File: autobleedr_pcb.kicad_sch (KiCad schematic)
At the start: 18 parts, among them J1 Barrel_Jack, J10 XT60 Connector, J11 Conn_01x02_Pin, J13 Screw_Terminal_01x08, J2 Conn_01x13_Pin, J3 Conn_01x14_Pin, J4 Conn_01x08_Socket, J7 Screw_Terminal_01x02, J8 Conn_01x02_Pin, J9 Conn_01x02_Pin

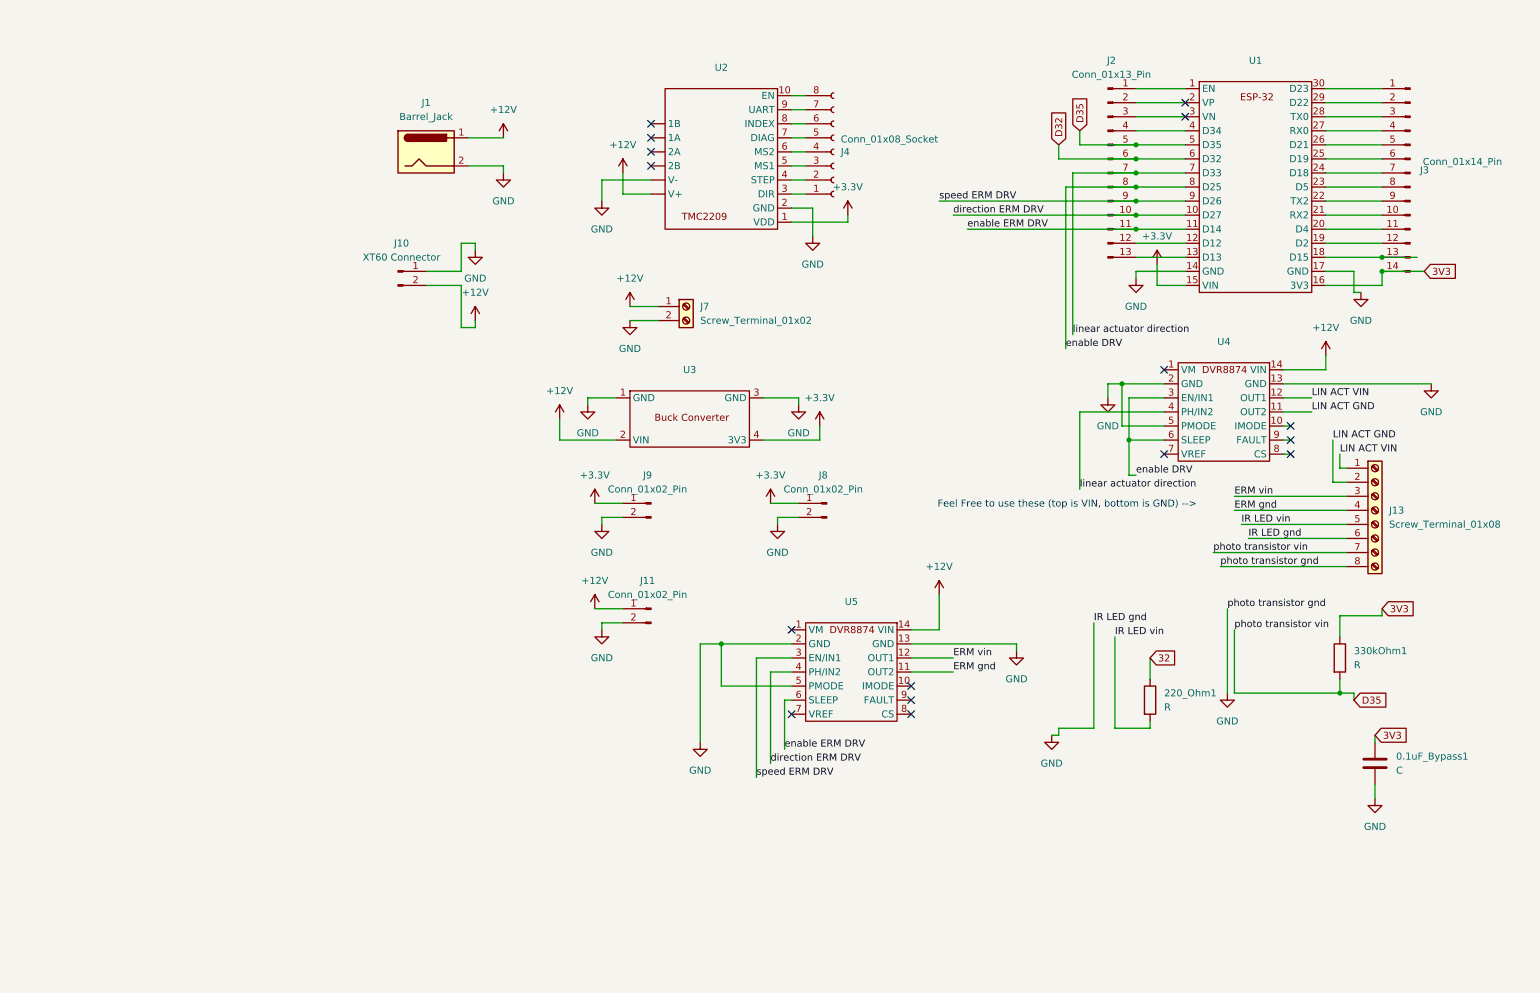
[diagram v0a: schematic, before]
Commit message: Redid symbols and footprints properly
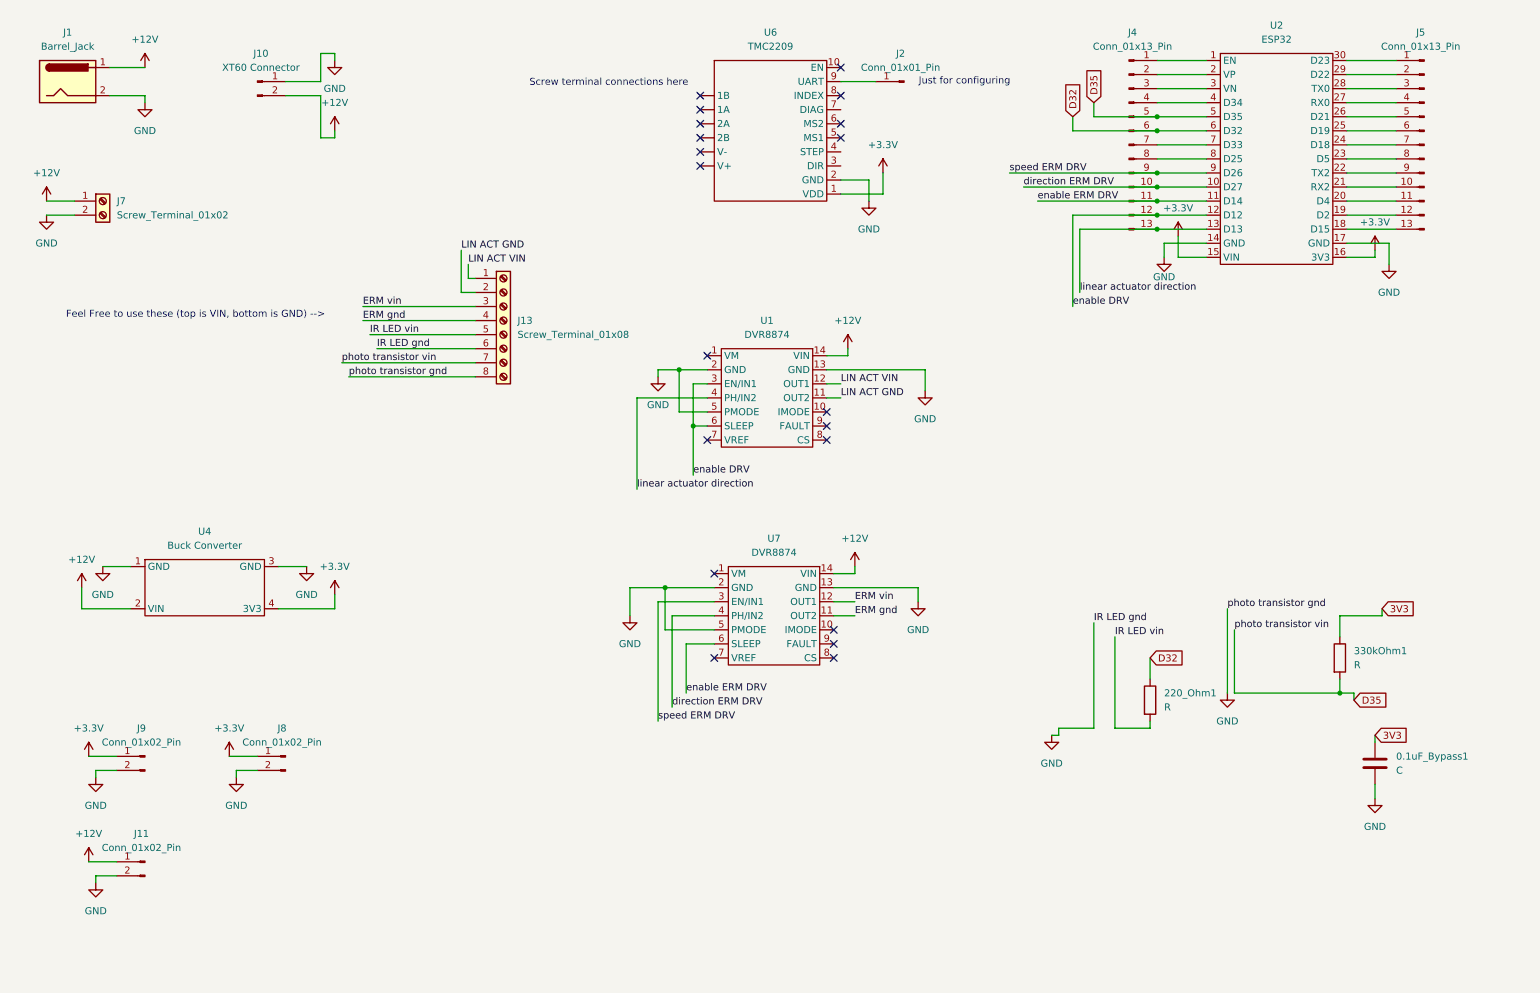
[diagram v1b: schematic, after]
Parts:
- removed J2: Conn_01x13_Pin, Connector_PinHeader_2.54mm:PinHeader_1x13_P2.54mm_Vertical, symbol Connector:Conn_01x13_Pin
- removed J3: Conn_01x14_Pin, Connector_PinHeader_2.54mm:PinHeader_1x14_P2.54mm_Vertical, symbol Connector:Conn_01x14_Pin
- removed J4: Conn_01x08_Socket, Connector_PinHeader_2.54mm:PinHeader_1x08_P2.54mm_Vertical, symbol Connector:Conn_01x08_Socket
- removed U1: ~, ESP-32:ESP-32, symbol ESP-32:ESP-32-Default
- removed U2: ~, Adafruit:TMC2209, symbol Adafruit:TMC2209
- removed U3: ~, Euogeudel:Buck Converter, symbol Euogeudel:Buck_Converter
- removed U4, U5: ~, Pololu:DVR8874, symbol Pololu:DRV8874
- added J2: Conn_01x01_Pin, Connector_PinHeader_2.54mm:PinHeader_1x01_P2.54mm_Vertical, symbol Connector:Conn_01x01_Pin
- added J4, J5: Conn_01x13_Pin, Connector_PinHeader_2.54mm:PinHeader_1x13_P2.54mm_Vertical, symbol Connector:Conn_01x13_Pin
- added U1, U7: DVR8874, Capstone_Footprints:DVR8874, symbol Capstone_Symbols:DVR8874
- added U2: ESP32, Capstone_Footprints:ESP32, symbol Capstone_Symbols:ESP32
- added U4: Buck Converter, Capstone_Footprints:Buck_Converter, symbol Capstone_Symbols:Buck_Converter
- added U6: TMC2209, Capstone_Footprints:TMC2209, symbol Capstone_Symbols:TMC2209
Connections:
- net 32 is gone; now on net D32: 220_Ohm1.1
- net +12V: now also U1.14 (VIN), U4.2 (VIN), U7.14 (VIN)
- net +3.3V: now also U2.15 (VIN), U2.16 (3V3), U4.4 (3V3), U6.1 (VDD)
- net D32: now also J4.6 (Pin_6), U2.6 (D32)
- net D35: now also J4.5 (Pin_5), U2.5 (D35)
- net ERM gnd: now also U7.11 (OUT2)
- net ERM vin: now also U7.12 (OUT1)
- net GND: now also U1.13 (GND), U1.2 (GND), U1.5 (PMODE), U2.14 (GND), U2.17 (GND), U4.1 (GND), U4.3 (GND), U6.2 (GND), U7.13 (GND), U7.2 (GND), U7.5 (PMODE)
- net LIN ACT GND: now also U1.11 (OUT2)
- net LIN ACT VIN: now also U1.12 (OUT1)
- net direction ERM DRV: now also J4.10 (Pin_10), U2.10 (D27), U7.4 (PH/IN2)
- net enable DRV: now also J4.12 (Pin_12), U1.3 (EN/IN1), U1.6 (SLEEP), U2.12 (D12)
- net enable ERM DRV: now also J4.11 (Pin_11), U2.11 (D14), U7.6 (SLEEP)
- net linear actuator direction: now also J4.13 (Pin_13), U1.4 (PH/IN2), U2.13 (D13)
- net speed ERM DRV: now also J4.9 (Pin_9), U2.9 (D26), U7.3 (EN/IN1)
- new net: J2.1 (Pin_1), U6.9 (UART)
- new net: J5.1 (Pin_1), U2.30 (D23)
- new net: J5.10 (Pin_10), U2.21 (RX2)
- new net: J5.11 (Pin_11), U2.20 (D4)
- new net: J5.12 (Pin_12), U2.19 (D2)
- new net: J5.13 (Pin_13), U2.18 (D15)
- new net: J5.2 (Pin_2), U2.29 (D22)
- new net: J5.3 (Pin_3), U2.28 (TX0)
- new net: J5.4 (Pin_4), U2.27 (RX0)
- new net: J5.5 (Pin_5), U2.26 (D21)
- new net: J5.6 (Pin_6), U2.25 (D19)
- new net: J5.7 (Pin_7), U2.24 (D18)
- new net: J5.8 (Pin_8), U2.23 (D5)
- new net: J5.9 (Pin_9), U2.22 (TX2)
- new net: J4.1 (Pin_1), U2.1 (EN)
- new net: J4.2 (Pin_2), U2.2 (VP)
- new net: J4.3 (Pin_3), U2.3 (VN)
- new net: J4.4 (Pin_4), U2.4 (D34)
- new net: J4.7 (Pin_7), U2.7 (D33)
- new net: J4.8 (Pin_8), U2.8 (D25)
- no-connect marks 16 -> 20
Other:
- note added: "Just for configuring"
- note added: "Screw terminal connections here"
- moved on the sheet: J1, J10, J11, J13, J7, J8, J9

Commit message: added Select Battery aka On Off Switch and power indicator LED with current limiting resistor
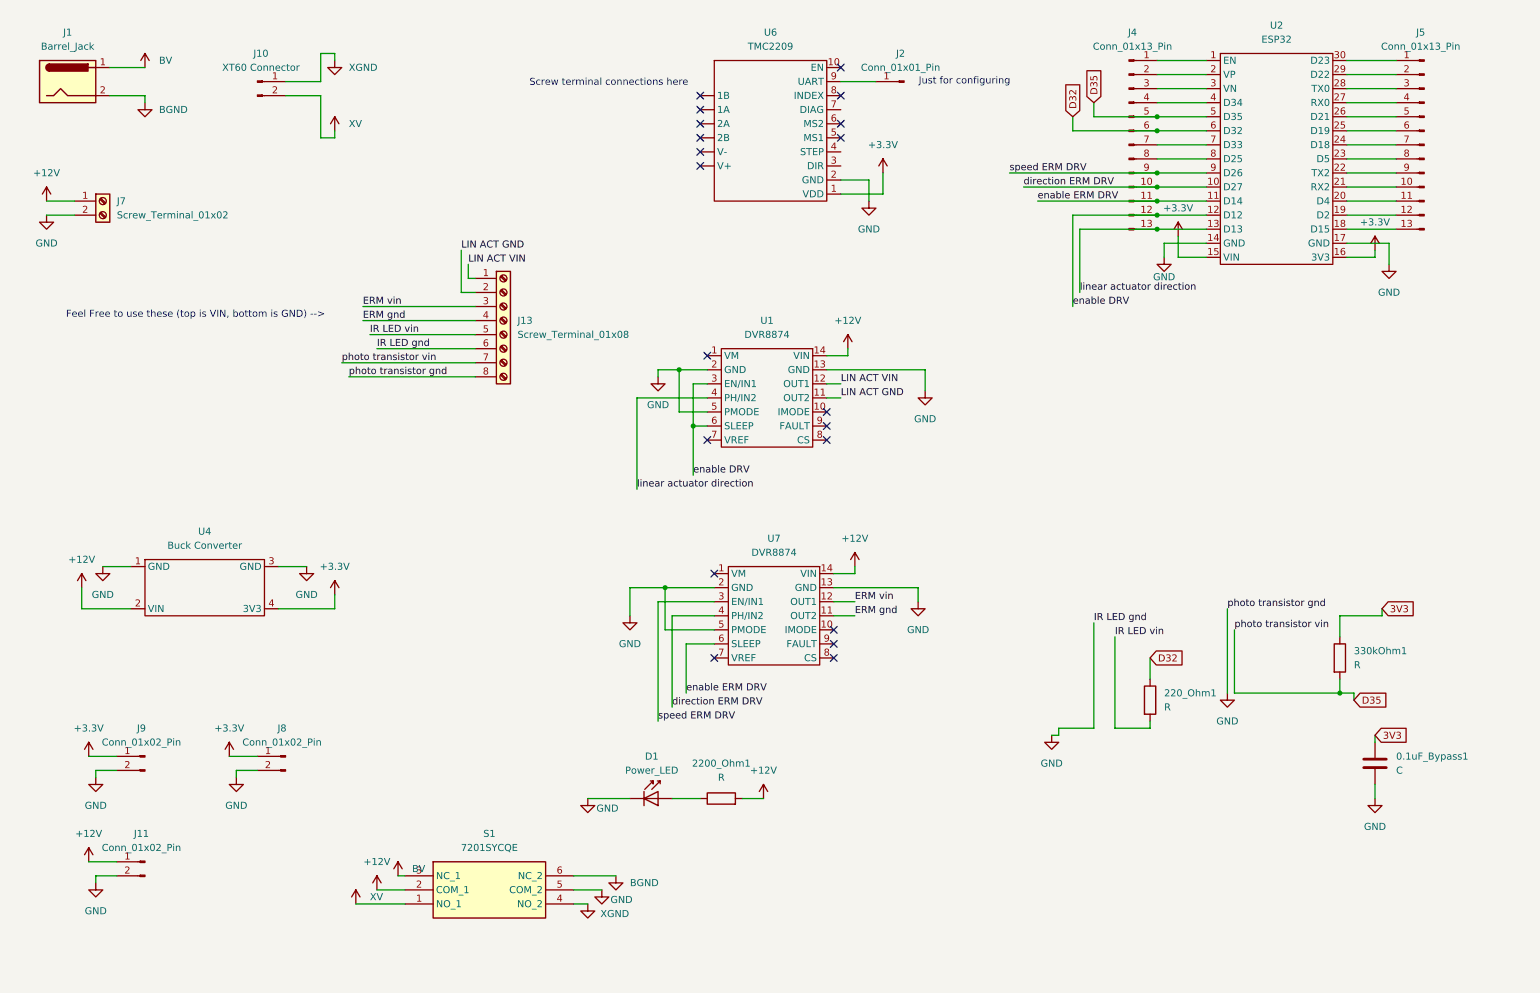
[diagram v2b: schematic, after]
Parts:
- added 2200_Ohm1: R, Resistor_THT:R_Axial_DIN0207_L6.3mm_D2.5mm_P7.62mm_Horizontal, symbol Device:R
- added D1: Power_LED, LED_THT:LED_D5.0mm_IRGrey, symbol LED:CQY99
- added S1: 7201SYCQE, 7201SYCQE, symbol Select_Battery_Switch:7201SYCQE
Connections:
- net +12V: now also 2200_Ohm1.2, S1.2 (COM_1); no longer J1.1, J10.2 (Pin_2)
- net GND: now also D1.1 (K), S1.5 (COM_2); no longer J1.2, J10.1 (Pin_1)
- new net: 2200_Ohm1.1, D1.2 (A)
- new net BGND: J1.2, S1.6 (NC_2)
- new net BV: J1.1, S1.3 (NC_1)
- new net XGND: J10.1 (Pin_1), S1.4 (NO_2)
- new net XV: J10.2 (Pin_2), S1.1 (NO_1)

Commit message: updated PCB
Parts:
- renumbered U7 to ERMU7, U1 to LinU1
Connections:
- net GND: now also U6.10 (EN)
- no-connect marks 20 -> 19
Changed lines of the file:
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@@
-	)
-	(no_connect
-		(at 163.83 27.94)
 	)
 	(no_connect
@@
 	(wire
 		(pts
+			(xy 166.37 19.05) (xy 167.64 19.05)
+		)
+		(stroke
+			(width 0)
+			(type default)
+		)
+	)
+	(wire
+		(pts
 			(xy 161.29 87.63) (xy 163.83 87.63)
 		)
@@
 	(wire
 		(pts
+			(xy 166.37 27.94) (xy 166.37 19.05)
+		)
+		(stroke
+			(width 0)
+			(type default)
+		)
+	)
+	(wire
+		(pts
 			(xy 205.74 54.61) (xy 220.98 54.61)
 		)
@@
 		(pts
 			(xy 234.95 129.54) (xy 234.95 140.97)
+		)
+		(stroke
+			(width 0)
+			(type default)
+		)
+	)
+	(wire
+		(pts
+			(xy 163.83 27.94) (xy 166.37 27.94)
 		)
 		(stroke
@@
 	)
 	(symbol
+		(lib_id "power:GND")
+		(at 167.64 19.05 90)
+		(unit 1)
+		(exclude_from_sim no)
+		(in_bom yes)
+		(on_board yes)
+		(dnp no)
+		(fields_autoplaced yes)
+		(property "Reference" "#PWR040"
+			(at 173.99 19.05 0)
+			(effects
+				(font
+					(size 1.27 1.27)
+				)
+				(hide yes)
+			)
+		)
+		(property "Value" "GND"
+			(at 171.45 19.0499 90)
+			(effects
+				(font
+					(size 1.27 1.27)
+				)
+				(justify right)
+			)
+		)
+		(property "Footprint" ""
+			(at 167.64 19.05 0)
+			(effects
+				(font
+					(size 1.27 1.27)
+				)
+				(hide yes)
+			)
+		)
+		(property "Datasheet" ""
+			(at 167.64 19.05 0)
+			(effects
+				(font
+					(size 1.27 1.27)
+				)
+				(hide yes)
+			)
+		)
+		(property "Description" "Power symbol creates a global label with name \"GND\" , ground"
+			(at 167.64 19.05 0)
+			(effects
+				(font
+					(size 1.27 1.27)
+				)
+				(hide yes)
+			)
+		)
+		(pin "1"
+		)
+		(instances
+			(project "autobleedr_pcb"
+				(path "/1cb070e6-4268-4590-be3a-70f1be021dfd"
+					(reference "#PWR040")
+					(unit 1)
+				)
+			)
+		)
+	)
+	(symbol
 		(lib_id "power:+12V")
 		(at 149.86 160.02 0)
@@
 		(dnp no)
 		(fields_autoplaced yes)
-		(property "Reference" "U1"
+		(property "Reference" "LinU1"
 			(at 150.495 73.66 0)
 			(effects
@@
 			(project ""
 				(path "/1cb070e6-4268-4590-be3a-70f1be021dfd"
-					(reference "U1")
+					(reference "LinU1")
 					(unit 1)
 				)
@@
 		(dnp no)
 		(fields_autoplaced yes)
-		(property "Reference" "U7"
+		(property "Reference" "ERMU7"
 			(at 151.765 113.03 0)
 			(effects
@@
 			(project ""
 				(path "/1cb070e6-4268-4590-be3a-70f1be021dfd"
-					(reference "U7")
+					(reference "ERMU7")
 					(unit 1)
 				)
